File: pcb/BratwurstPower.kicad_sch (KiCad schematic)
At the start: 38 parts, among them J1 BarrelJack, J10 GPIO, J2 Raspi, J3 USB1in, J4 USB1out, J5 I2C, J6 I2C, J7 USB2in, J8 USB2out, J9 EXT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

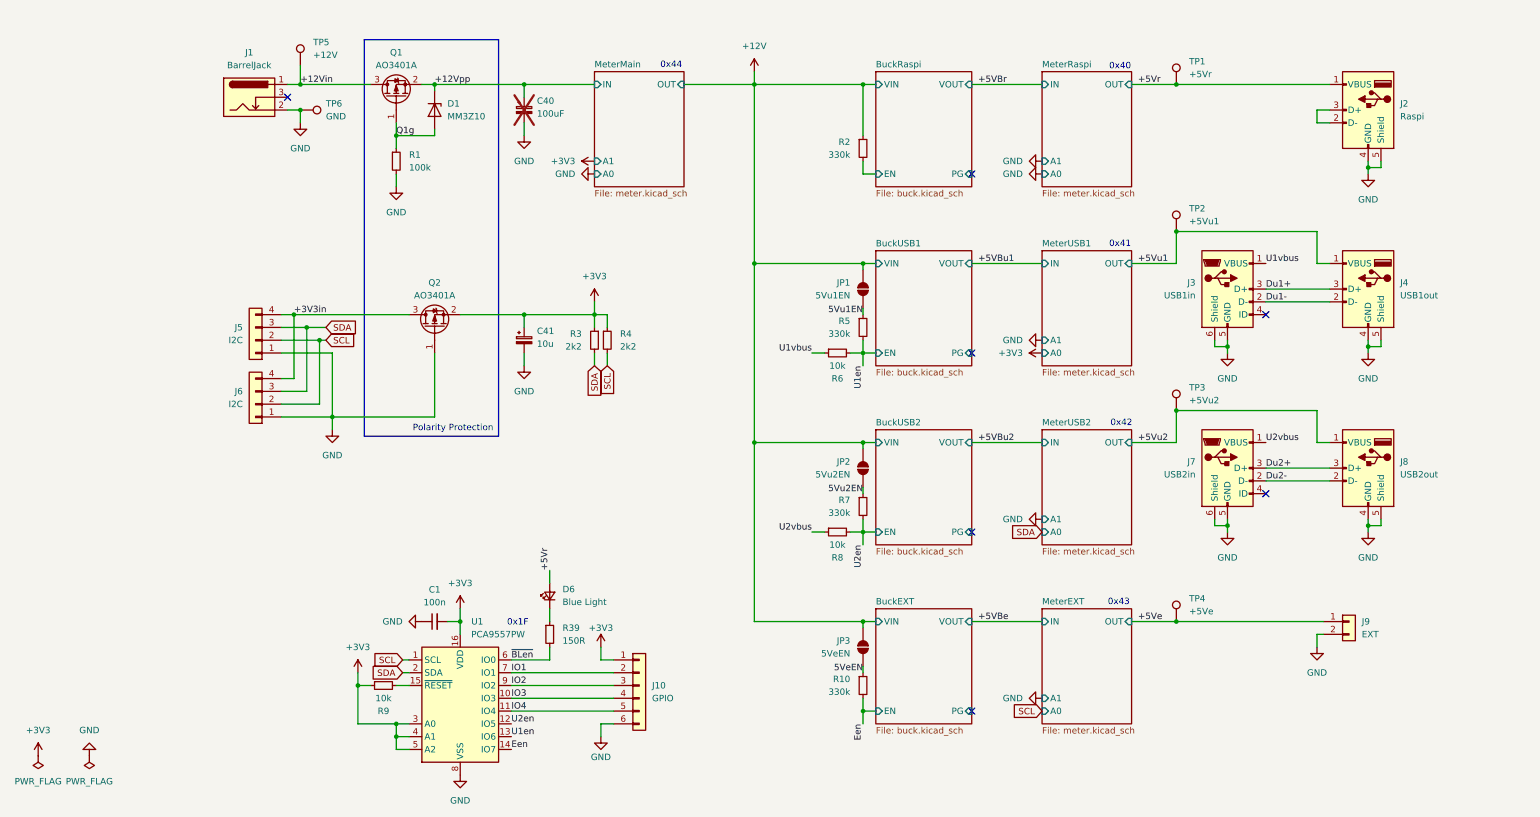
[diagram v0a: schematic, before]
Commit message: feat!: Replace USB mini and Raspi port with USB-C
feat: add connector for USB OTG connection
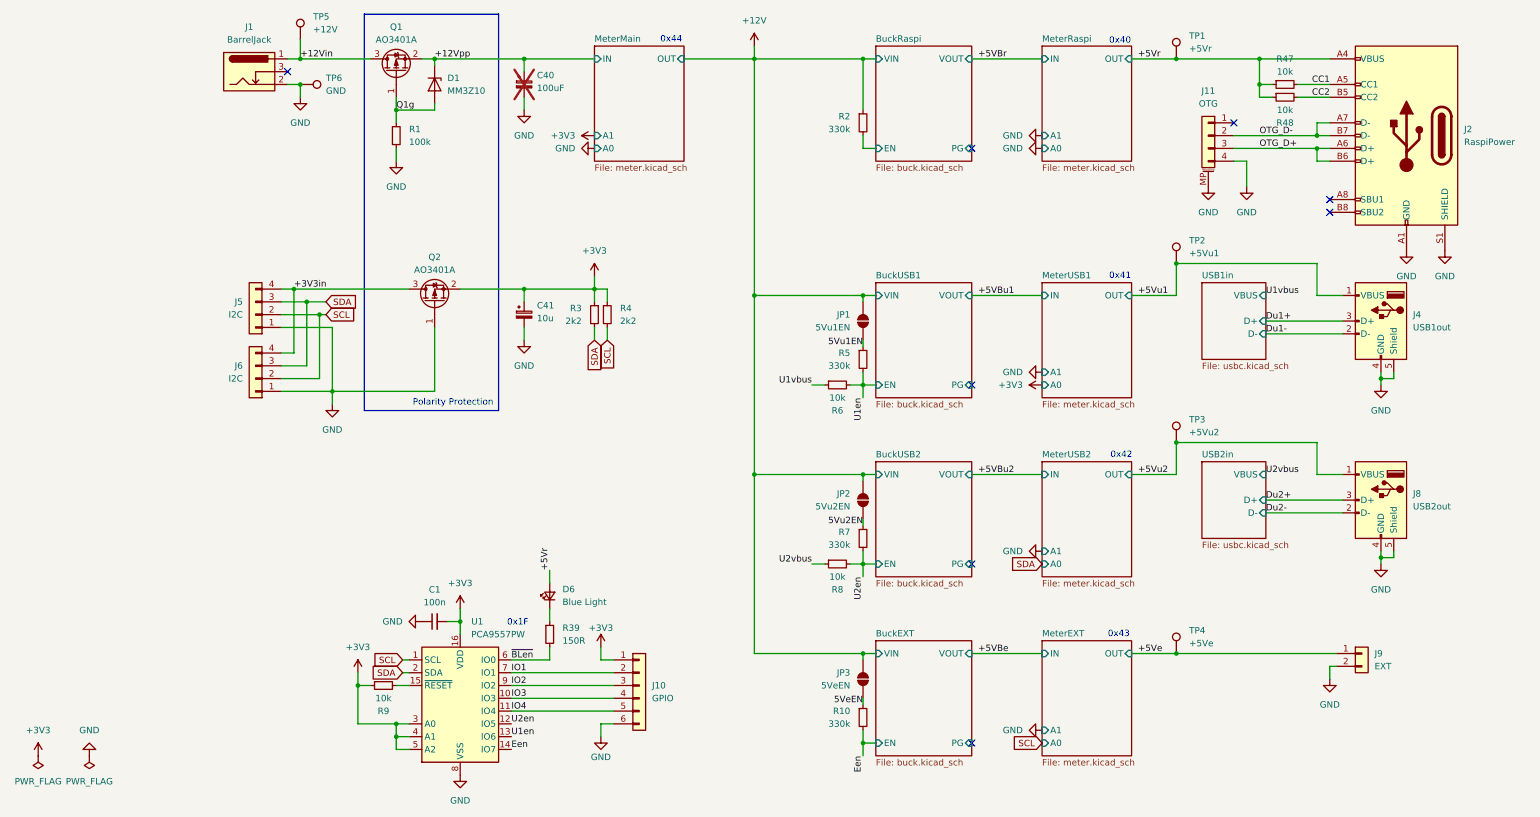
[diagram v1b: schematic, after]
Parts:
- removed J2: Raspi, Connector_USB:USB_A_Molex_67643_Horizontal, symbol Connector:USB_A
- removed J3: USB1in, BratwurstPower:Connector_USB_Mini_THT, symbol Connector:USB_B_Mini
- removed J7: USB2in, BratwurstPower:Connector_USB_Mini_THT, symbol Connector:USB_B_Mini
- added J11: OTG, Connector_JST:JST_SH_SM04B-SRSS-TB_1x04-1MP_P1.00mm_Horizontal, symbol Connector_Generic_MountingPin:Conn_01x04_MountingPin
- added J2: RaspiPower, Connector_USB:USB_C_Receptacle_GCT_USB4105-xx-A_16P_TopMnt_Horizontal, symbol Connector:USB_C_Receptacle_USB2.0_16P
- added R47, R48: 10k, Resistor_SMD:R_0402_1005Metric, symbol Device:R_Small
- J4, J8: LCSC (none) -> C2798029
- J5, J6: LCSC (none) -> C265452
- J9: LCSC (none) -> C157931
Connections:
- net +5Vr: now also J2.A4 (VBUS), J2.A9 (VBUS), J2.B4 (VBUS), J2.B9 (VBUS), R47.1, R48.1
- net GND: now also J11.4 (Pin_4), J11.MP (MountPin), J2.A1 (GND), J2.A12 (GND), J2.B1 (GND), J2.B12 (GND), J2.S1 (SHIELD)
- new net CC1: J2.A5 (CC1), R47.2
- new net CC2: J2.B5 (CC2), R48.2
- new net OTG_D+: J11.3 (Pin_3), J2.A6 (D+), J2.B6 (D+)
- new net OTG_D-: J11.2 (Pin_2), J2.A7 (D-), J2.B7 (D-)
- no-connect marks 7 -> 8
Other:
- added sheet USB1in (usbc.kicad_sch)
- added sheet USB2in (usbc.kicad_sch)
- moved on the sheet: C40, C41, D1, J1, J4, J5, J6, J8, J9, JP1, JP2, JP3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

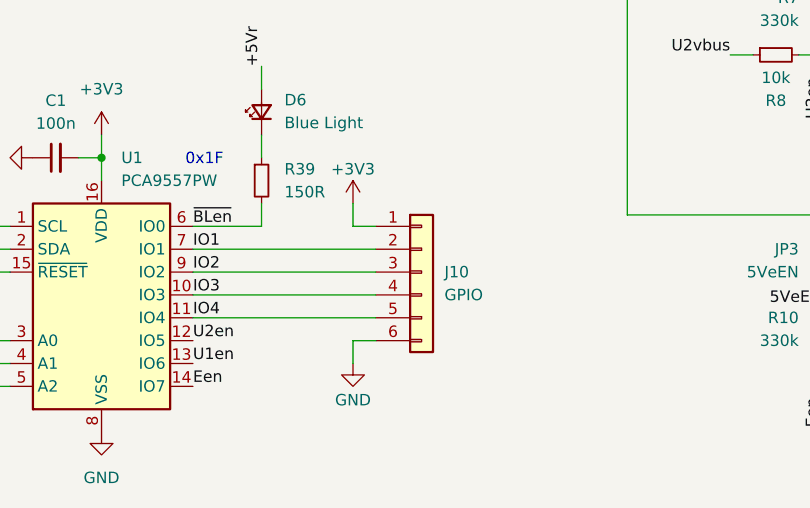
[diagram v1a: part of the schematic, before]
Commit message: style: replace OTG connector
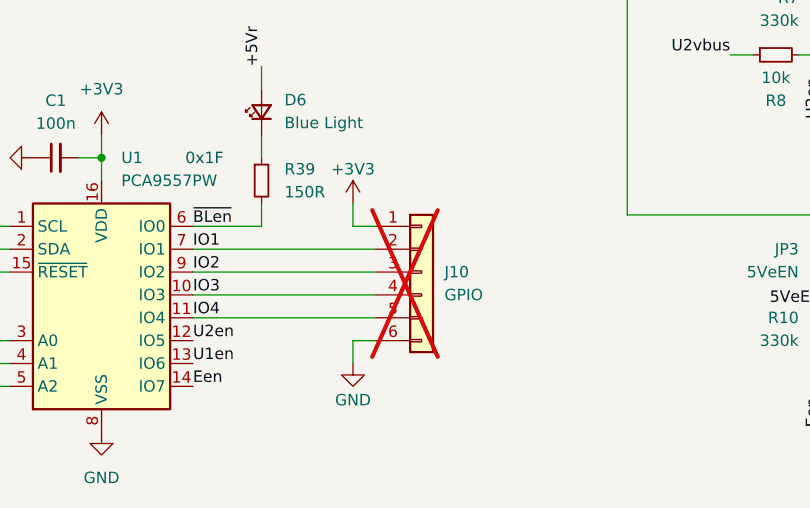
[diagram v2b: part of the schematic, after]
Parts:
- J10: now not fitted
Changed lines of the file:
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@@
 		(in_bom yes)
 		(on_board yes)
-		(dnp no)
+		(dnp yes)
 		(fields_autoplaced yes)
 		(property "Reference" "J10"

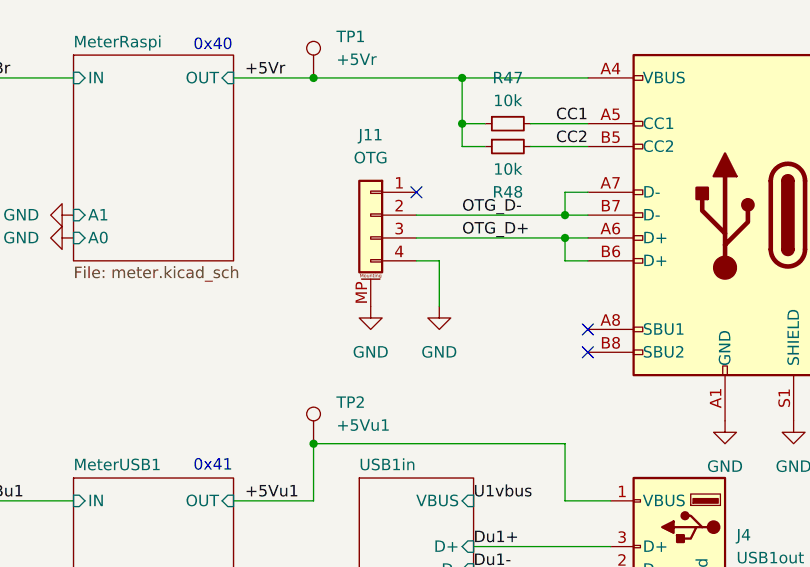
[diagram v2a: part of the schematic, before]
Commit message: style: replace OTG connector
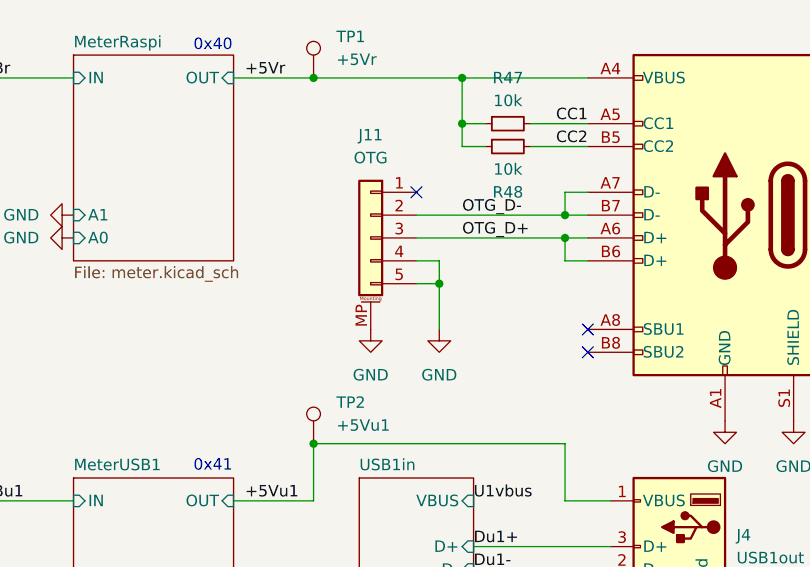
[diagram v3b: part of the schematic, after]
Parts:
- J11: footprint Connector_JST:JST_SH_SM04B-SRSS-TB_1x04-1MP_P1.00mm_Horizontal -> Connector_JST:JST_SH_SM05B-SRSS-TB_1x05-1MP_P1.00mm_Horizontal; symbol Connector_Generic_MountingPin:Conn_01x04_MountingPin -> Connector_Generic_MountingPin:Conn_01x05_MountingPin
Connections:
- net GND: now also J11.5 (Pin_5)
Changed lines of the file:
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@@
 	)
 	(junction
+		(at 219.71 46.99)
+		(diameter 0)
+		(color 0 0 0 0)
+	)
+	(junction
 		(at 33.02 72.39)
 		(diameter 0)
@@
 	(wire
 		(pts
-			(xy 219.71 49.53) (xy 219.71 44.45)
+			(xy 219.71 52.07) (xy 219.71 46.99)
 		)
 		(stroke
@@
 	(wire
 		(pts
-			(xy 219.71 44.45) (xy 217.17 44.45)
+			(xy 219.71 46.99) (xy 217.17 46.99)
 		)
 		(stroke
@@
 	(wire
 		(pts
+			(xy 217.17 44.45) (xy 219.71 44.45)
+		)
+		(stroke
+			(width 0)
+			(type default)
+		)
+	)
+	(wire
+		(pts
 			(xy 143.51 24.13) (xy 146.05 24.13)
 		)
@@
 	(wire
 		(pts
+			(xy 219.71 44.45) (xy 219.71 46.99)
+		)
+		(stroke
+			(width 0)
+			(type default)
+		)
+	)
+	(wire
+		(pts
 			(xy 143.51 160.02) (xy 146.05 160.02)
 		)
@@
 	)
 	(symbol
-		(lib_id "Connector_Generic_MountingPin:Conn_01x04_MountingPin")
-		(at 212.09 39.37 0)
+		(lib_id "Connector_Generic_MountingPin:Conn_01x05_MountingPin")
+		(at 212.09 41.91 0)
 		(mirror y)
 		(unit 1)
@@
 			)
 		)
-		(property "Footprint" "Connector_JST:JST_SH_SM04B-SRSS-TB_1x04-1MP_P1.00mm_Horizontal"
-			(at 212.09 39.37 0)
+		(property "Footprint" "Connector_JST:JST_SH_SM05B-SRSS-TB_1x05-1MP_P1.00mm_Horizontal"
+			(at 212.09 41.91 0)
 			(effects
 				(font
@@
 		)
 		(property "Datasheet" "~"
-			(at 212.09 39.37 0)
+			(at 212.09 41.91 0)
 			(effects
 				(font
@@
 			)
 		)
-		(property "Description" "Generic connectable mounting pin connector, single row, 01x04, script generated (kicad-library-utils/schlib/autogen/connector/)"
-			(at 212.09 39.37 0)
+		(property "Description" "Generic connectable mounting pin connector, single row, 01x05, script generated (kicad-library-utils/schlib/autogen/connector/)"
+			(at 212.09 41.91 0)
 			(effects
 				(font
@@
 		)
 		(property "LCSC" "C160404"
-			(at 212.09 39.37 0)
+			(at 212.09 41.91 0)
 			(effects
 				(font
@@
 		(pin "MP"
 		)
+		(pin "5"
+		)
 		(instances
 			(project ""
@@
 	(symbol
 		(lib_id "power:GND")
-		(at 219.71 49.53 0)
+		(at 219.71 52.07 0)
 		(unit 1)
 		(exclude_from_sim no)
@@
 		(fields_autoplaced yes)
 		(property "Reference" "#PWR054"
-			(at 219.71 55.88 0)
+			(at 219.71 58.42 0)
 			(effects
 				(font
@@
 		)
 		(property "Value" "GND"
-			(at 219.71 54.61 0)
+			(at 219.71 57.15 0)
 			(effects
 				(font
@@
 		)
 		(property "Footprint" ""
-			(at 219.71 49.53 0)
+			(at 219.71 52.07 0)
 			(effects
 				(font
@@
 		)
 		(property "Datasheet" ""
-			(at 219.71 49.53 0)
+			(at 219.71 52.07 0)
 			(effects
 				(font
@@
 		)
 		(property "Description" "Power symbol creates a global label with name \"GND\" , ground"
-			(at 219.71 49.53 0)
+			(at 219.71 52.07 0)
 			(effects
 				(font
@@
 	(symbol
 		(lib_id "power:GND")
-		(at 212.09 49.53 0)
+		(at 212.09 52.07 0)
 		(unit 1)
 		(exclude_from_sim no)
@@
 		(fields_autoplaced yes)
 		(property "Reference" "#PWR049"
-			(at 212.09 55.88 0)
+			(at 212.09 58.42 0)
 			(effects
 				(font
@@
 		)
 		(property "Value" "GND"
-			(at 212.09 54.61 0)
+			(at 212.09 57.15 0)
 			(effects
 				(font
@@
 		)
 		(property "Footprint" ""
-			(at 212.09 49.53 0)
+			(at 212.09 52.07 0)
 			(effects
 				(font
@@
 		)
 		(property "Datasheet" ""
-			(at 212.09 49.53 0)
+			(at 212.09 52.07 0)
 			(effects
 				(font
@@
 		)
 		(property "Description" "Power symbol creates a global label with name \"GND\" , ground"
-			(at 212.09 49.53 0)
+			(at 212.09 52.07 0)
 			(effects
 				(font

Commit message: chore: cleanup
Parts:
- D6: footprint LED_SMD:LED_0805_2012Metric -> LED_SMD:LED_0603_1608Metric_Pad1.05x0.95mm_HandSolder
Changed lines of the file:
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@@
 	(wire
 		(pts
+			(xy 177.8 124.46) (xy 179.07 124.46)
+		)
+		(stroke
+			(width 0)
+			(type default)
+		)
+	)
+	(wire
+		(pts
 			(xy 33.02 85.09) (xy 33.02 72.39)
 		)
@@
 	(wire
 		(pts
+			(xy 177.8 160.02) (xy 179.07 160.02)
+		)
+		(stroke
+			(width 0)
+			(type default)
+		)
+	)
+	(wire
+		(pts
 			(xy 53.34 161.29) (xy 50.8 161.29)
 		)
@@
 	(global_label "SCL"
 		(shape input)
-		(at 179.07 160.02 180)
+		(at 177.8 160.02 180)
 		(fields_autoplaced yes)
 		(effects
@@
 		)
 		(property "Intersheetrefs" "${INTERSHEET_REFS}"
-			(at 172.5772 160.02 0)
+			(at 171.3072 160.02 0)
 			(effects
 				(font
@@
 	(global_label "SDA"
 		(shape input)
-		(at 179.07 124.46 180)
+		(at 177.8 124.46 180)
 		(fields_autoplaced yes)
 		(effects
@@
 		)
 		(property "Intersheetrefs" "${INTERSHEET_REFS}"
-			(at 172.5167 124.46 0)
+			(at 171.2467 124.46 0)
 			(effects
 				(font
@@
 			)
 		)
-		(property "Footprint" "LED_SMD:LED_0805_2012Metric"
+		(property "Footprint" "LED_SMD:LED_0603_1608Metric_Pad1.05x0.95mm_HandSolder"
 			(at 81.28 130.81 90)
 			(effects

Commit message: fix: part numbers
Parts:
- C41: LCSC (none) -> C7171
- D6: LCSC C375547 -> C72041
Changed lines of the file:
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@@
+			)
+		)
+		(property "LCSC" "C7171"
+			(at 76.2 74.93 0)
+			(effects
+				(font
+					(size 1.27 1.27)
+				)
+				(hide yes)
 			)
 		)
@@
 			)
 		)
-		(property "LCSC" "C375547"
+		(property "LCSC" "C72041"
 			(at 81.28 130.81 0)
 			(effects

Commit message: feat: add 3.3V LDO for I2C circuitry
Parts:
- removed C41: 10u, Capacitor_Tantalum_SMD:CP_EIA-3216-18_Kemet-A, symbol Device:C_Polarized_Small
- removed Q2: AO3401A, Package_TO_SOT_SMD:SOT-23, symbol Transistor_FET:AO3401A
- added C41, C42: 1u, Capacitor_SMD:C_0402_1005Metric, symbol Device:C_Small
- added U11: XC6206P332MR-G, Package_TO_SOT_SMD:SOT-23-3, symbol Regulator_Linear:XC6206PxxxMR
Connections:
- net +3V3: now also C42.1, U11.2 (VO)
- net +5Vr: now also C41.1, U11.3 (VI)
- net GND: now also C41.2, C42.2, U11.1 (GND)
- net +3V3in renamed +3V3_I2C
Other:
- moved on the sheet: R3, R4

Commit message: fix: change pots to 2.2kΩ
fix: part numbers
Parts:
- C41, C42: LCSC (none) -> C52923
- Q1: value AO3401A -> HL3415A; LCSC C15127 -> C28646270
- R3, R4: LCSC C25890 -> C25879
- U11: LCSC (none) -> C5446
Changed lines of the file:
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@@
 			)
 		)
+		(property "LCSC" "C52923"
+			(at 88.9 74.93 0)
+			(effects
+				(font
+					(size 1.27 1.27)
+				)
+				(hide yes)
+			)
+		)
 		(pin "2"
 		)
@@
 			)
 		)
+		(property "LCSC" "C52923"
+			(at 68.58 74.93 0)
+			(effects
+				(font
+					(size 1.27 1.27)
+				)
+				(hide yes)
+			)
+		)
 		(pin "2"
 		)
@@
 			)
 		)
+		(property "LCSC" "C5446"
+			(at 78.74 69.85 0)
+			(effects
+				(font
+					(size 1.27 1.27)
+				)
+				(hide yes)
+			)
+		)
 		(pin "1"
 		)
@@
 			)
 		)
-		(property "Value" "AO3401A"
+		(property "Value" "HL3415A"
 			(at 50.8 20.32 90)
 			(effects
@@
 			)
 		)
-		(property "Datasheet" "http://www.aosmd.com/pdfs/datasheet/AO3401A.pdf"
+		(property "Datasheet" "https://wmsc.lcsc.com/wmsc/upload/file/pdf/v2/lcsc/2407121622_hongjiacheng-HL3415A_C28646270.pdf"
 			(at 54.61 21.59 0)
 			(effects
@@
 			)
 		)
-		(property "LCSC" "C15127"
+		(property "LCSC" "C28646270"
 			(at 50.8 26.67 0)
 			(effects
@@
 			)
 		)
-		(property "LCSC" "C25890"
+		(property "LCSC" "C25879"
 			(at 105.41 74.93 0)
 			(effects
@@
 			)
 		)
-		(property "LCSC" "C25890"
+		(property "LCSC" "C25879"
 			(at 102.87 74.93 0)
 			(effects

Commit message: feat: optional connection RaspiEN to IO1
In case external control of the I2C bus is taken, this can be used to hard-reset the Raspberry Pi
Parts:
- added JP4: RaspiEN, Jumper:SolderJumper-2_P1.3mm_Open_TrianglePad1.0x1.5mm, symbol Jumper:SolderJumper_2_Open
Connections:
- net BuckRaspi/EN: now also JP4.2 (B)
- net IO1: now also JP4.1 (A)
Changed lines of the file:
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@@
 	)
 	(junction
+		(at 143.51 41.91)
+		(diameter 0)
+		(color 0 0 0 0)
+	)
+	(junction
 		(at 246.38 123.19)
 		(diameter 0)
@@
 	(wire
 		(pts
+			(xy 143.51 52.07) (xy 143.51 54.61)
+		)
+		(stroke
+			(width 0)
+			(type default)
+		)
+	)
+	(wire
+		(pts
 			(xy 217.17 39.37) (xy 233.68 39.37)
 		)
@@
 	(wire
 		(pts
+			(xy 143.51 41.91) (xy 143.51 44.45)
+		)
+		(stroke
+			(width 0)
+			(type default)
+		)
+	)
+	(wire
+		(pts
 			(xy 50.8 34.29) (xy 50.8 36.83)
 		)
@@
 		)
 	)
+	(label "IO1"
+		(at 143.51 54.61 270)
+		(fields_autoplaced yes)
+		(effects
+			(font
+				(size 1.27 1.27)
+			)
+			(justify right bottom)
+		)
+	)
 	(label "IO3"
 		(at 73.66 151.13 0)
@@
 					(unit 1)
 				)
+			)
+		)
+	)
+	(symbol
+		(lib_id "Jumper:SolderJumper_2_Open")
+		(at 143.51 48.26 270)
+		(mirror x)
+		(unit 1)
+		(exclude_from_sim yes)
+		(in_bom no)
+		(on_board yes)
+		(dnp no)
+		(property "Reference" "JP4"
+			(at 140.97 46.9899 90)
+			(effects
+				(font
+					(size 1.27 1.27)
+				)
+				(justify right)
+			)
+		)
+		(property "Value" "RaspiEN"
+			(at 140.97 49.5299 90)
+			(effects
+				(font
+					(size 1.27 1.27)
+				)
+				(justify right)
+			)
+		)
+		(property "Footprint" "Jumper:SolderJumper-2_P1.3mm_Open_TrianglePad1.0x1.5mm"
+			(at 143.51 48.26 0)
+			(effects
+				(font
+					(size 1.27 1.27)
+				)
+				(hide yes)
+			)
+		)
+		(property "Datasheet" "~"
+			(at 143.51 48.26 0)
+			(effects
+				(font
+					(size 1.27 1.27)
+				)
+				(hide yes)
+			)
+		)
+		(property "Description" "Solder Jumper, 2-pole, open"
+			(at 143.51 48.26 0)
+			(effects
+				(font
+					(size 1.27 1.27)
+				)
+				(hide yes)
+			)
+		)
+		(pin "2"
+		)
+		(pin "1"
+		)
+		(instances
+			(project "BratwurstPower"
+				(path "/d3b20f0a-e666-4f64-bba3-6679d961a6dd"
+					(reference "JP4")
+					(unit 1)
+				)
